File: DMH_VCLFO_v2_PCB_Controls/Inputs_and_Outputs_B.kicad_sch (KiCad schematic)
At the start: 40 parts, among them J10 TS_Jack_6.35mm_Sw, J11 TS_Jack_6.35mm_Sw, J12 TS_Jack_6.35mm_Sw, J24 Conn_01x08, J25 Conn_01x08, J27 Conn_01x08, J28 Conn_01x08, J7 TS_Jack_6.35mm_Sw, J8 TS_Jack_6.35mm_Sw, J9 TS_Jack_6.35mm_Sw, Q3 BC548, Q4 BC558, SW5 SW_SPDT, SW6 SPDT_OnOffOn, SW7 SW_SPDT, SW8 SW_SPDT, U2 TL074

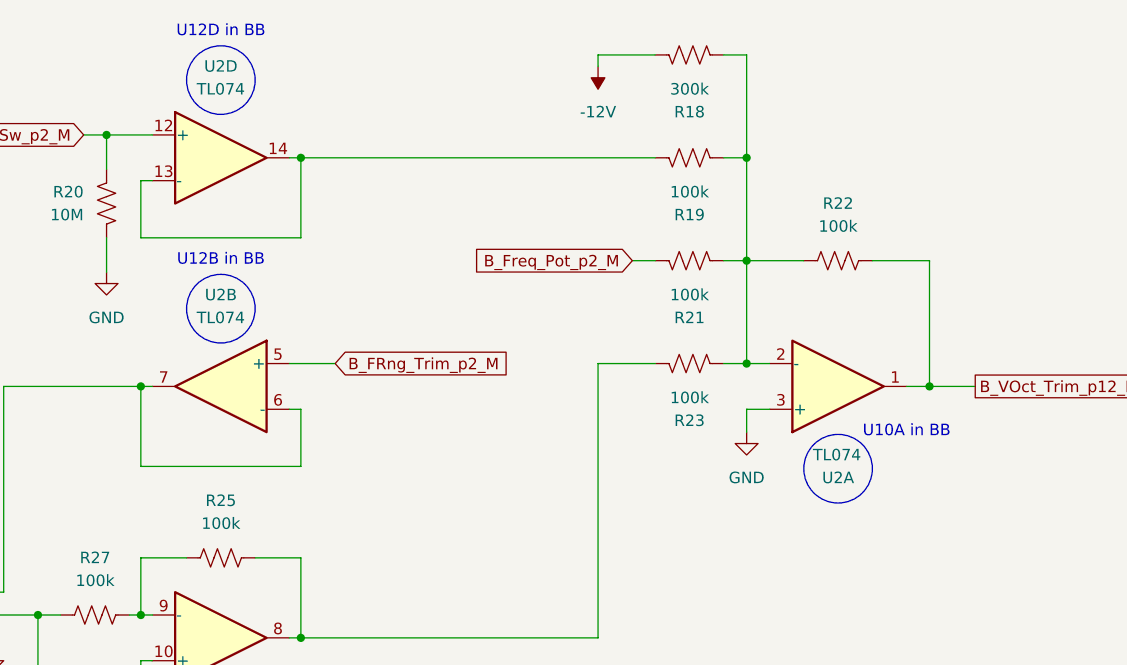
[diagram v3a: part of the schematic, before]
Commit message: Added project with Single VCLFO schematic
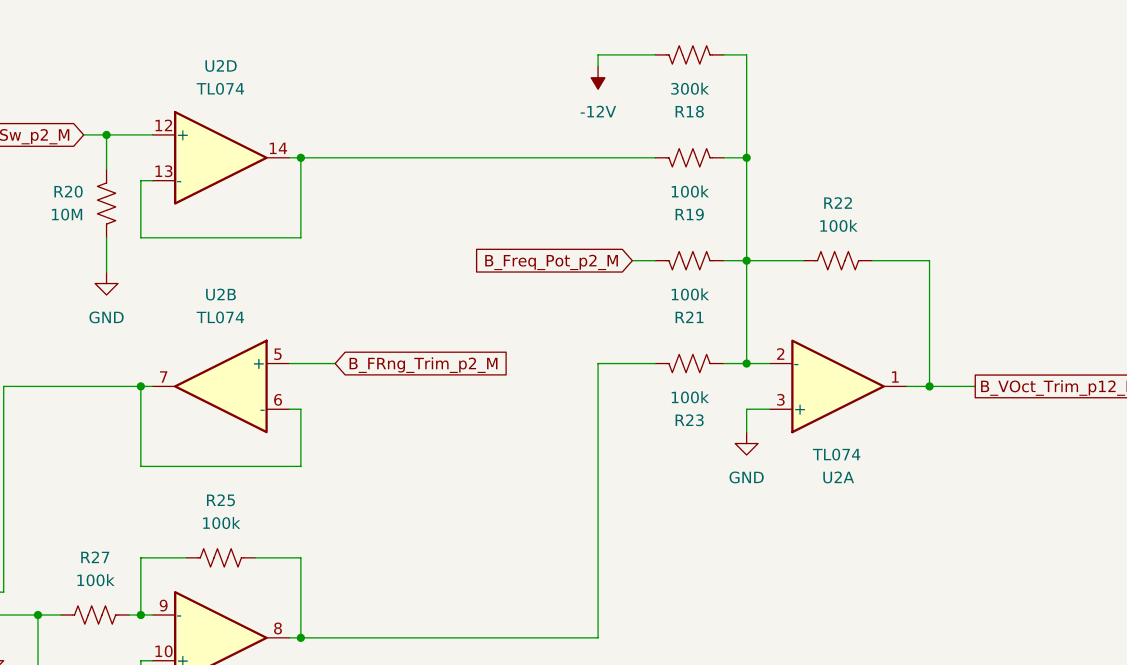
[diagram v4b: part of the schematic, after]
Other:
- note removed: "U10A in BB"
- note removed: "U12B in BB"
- note removed: "U12D in BB"
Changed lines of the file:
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@@
 		(comment 1 "PCB for 10cm Kosmo format synthesizer module")
-	)
-	(circle
-		(center 236.22 66.294)
-		(radius 3.81)
-		(stroke
-			(width 0)
-			(type default)
-		)
-		(fill
-			(type none)
-		)
-	)
-	(circle
-		(center 167.64 48.514)
-		(radius 3.81)
-		(stroke
-			(width 0)
-			(type default)
-		)
-		(fill
-			(type none)
-		)
-	)
-	(circle
-		(center 167.64 23.114)
-		(radius 3.81)
-		(stroke
-			(width 0)
-			(type default)
-		)
-		(fill
-			(type none)
-		)
-	)
-	(text "U12B in BB"
-		(exclude_from_sim no)
-		(at 167.64 43.18 0)
-		(effects
-			(font
-				(size 1.27 1.27)
-			)
-		)
-	)
-	(text "U10A in BB"
-		(exclude_from_sim no)
-		(at 243.84 62.23 0)
-		(effects
-			(font
-				(size 1.27 1.27)
-			)
-		)
-	)
-	(text "U12D in BB"
-		(exclude_from_sim no)
-		(at 167.64 17.78 0)
-		(effects
-			(font
-				(size 1.27 1.27)
-			)
-		)
 	)
 	(junction
